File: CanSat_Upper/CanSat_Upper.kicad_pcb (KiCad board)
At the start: 2 copper layers, 50 x 50 mm, 33 parts, among them J1 SERVO1, J10 Power GND, J2 SERVO1, J3 SERVO1, J4 SERVO1, J5 SERVO1, J6 SERVO1, J7 Power 5V, J8 JST_SH_10pin, J9 JST_SH_8pin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

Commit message: LDO and gps early layout done
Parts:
- moved C6 81.3 mm to (263.8, 132.8)
- moved C5 78.2 mm to (260.8, 132.8), turned to 180 degrees
- moved C8 52.1 mm to (242.8, 91.8)
- moved C7 49.7 mm to (240.4, 107.0)
- moved C3 47.1 mm to (229.8, 121.4), turned to 180 degrees
- moved C4 43.2 mm to (226.6, 121.4)
- moved C1 42.0 mm to (220.6, 121.4), turned to 180 degrees
- moved R4 40.9 mm to (235.2, 93.4)
- moved C9 39.8 mm to (231.2, 106.0)
- moved C2 37.9 mm to (217.4, 121.4)
- moved R2 36.8 mm to (225.8, 119.0), turned to -90 degrees
- moved R3 35.4 mm to (229.8, 91.8)
- moved R1 31.5 mm to (216.6, 119.0), turned to -90 degrees
- moved U5 10.8 mm to (228.2, 119.0)
- moved U1 9.56 mm to (235.9, 100.3)
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
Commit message: general PBC layout done
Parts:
- removed C10: 100n, Capacitor_SMD:C_0603_1608Metric
- removed R2: 10k, Resistor_SMD:R_0603_1608Metric
- removed U5: LP5912_500-ma/3.3V, LDO:LP5912-LDO
- added D1: TVS, Diode_SMD:D_0402_1005Metric, F.Cu at (111.0, 100.4)
- added D2: TVS, Diode_SMD:D_0402_1005Metric, F.Cu at (112.2, 101.4)
- added D3: TVS, Diode_SMD:D_0402_1005Metric, F.Cu at (110.0, 103.6)
- added D4: TVS, Diode_SMD:D_0402_1005Metric, F.Cu at (111.0, 104.6)
- C3: value 10u -> 1u
- C4: value 10u -> 8.2p
- J10, J7: footprint Connector_Wire:SolderWirePad_1x01_SMD_4x8mm -> Connector_Wire:SolderWirePad_1x01_SMD_3x6mm
- moved C6 141.1 mm to (129.8, 88.5), turned to 180 degrees
- moved C5 135.1 mm to (133.2, 88.5), turned to 0 degrees
- moved C8 128.6 mm to (114.2, 93.6), turned to 90 degrees
- moved C7 123.5 mm to (117.8, 92.6)
- moved R4 122.7 mm to (112.5, 94.8), turned to -90 degrees
- moved C3 121.1 mm to (122.4, 65.4), turned to 90 degrees
- moved U1 119.3 mm to (116.8, 95.1), turned to 90 degrees
- moved J9 118.2 mm to (102.8, 71.4), turned to -90 degrees
- moved R3 117.5 mm to (112.5, 98.0), turned to 90 degrees
- moved C4 116.8 mm to (122.4, 68.6), turned to -90 degrees
- moved J8 116.2 mm to (103.0, 98.2), turned to -90 degrees
- moved C9 114.0 mm to (117.5, 97.6)
- moved U3 113.8 mm to (143.7, 90.5), turned to 180 degrees
- moved C1 110.2 mm to (116.4, 85.6), turned to -90 degrees
- moved U4 109.7 mm to (114.0, 87.2), turned to 90 degrees
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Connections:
- C2 pad 1: +3.3V1 -> +3.3V
- C3 pad 1: +5V -> +3.3V
- C4 pad 1: +3.3V2 -> +3.3V
- C5 pad 1: +3.3V1 -> +3.3V
- C6 pad 1: +3.3V1 -> +3.3V
- C8 pad 1: +3.3V2 -> +3.3V
- C9 pad 1: +3.3V2 -> +3.3V
- J8 pad 8: /GPS_TX -> /GPS_RX
- J8 pad 9: /GPS_RX -> /GPS_TX
- R1 pad 2: +3.3V1 -> +3.3V
- R3 pad 1: +3.3V2 -> +3.3V
- R4 pad 1: +3.3V2 -> +3.3V
- U1 pad 13: +3.3V2 -> +3.3V
- U1 pad 2: +3.3V2 -> +3.3V
- U2 pad 1: +3.3V2 -> +3.3V
- U3 pad 52: +3.3V1 -> +3.3V
- U3 pad 53: +3.3V1 -> +3.3V
- U4 pad 1: +3.3V1 -> +3.3V
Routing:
- net +3.3V: track 0.00 -> 91.3 mm
- net /XBEE_TX: track 0.00 -> 49.4 mm
- net /XBEE_RX: track 0.00 -> 49.3 mm
- net /GPS_TX: track 0.00 -> 23.6 mm
- net /GPS_RX: track 0.00 -> 23.3 mm
- net /S4: track 0.00 -> 12.2 mm
- net /S3: track 0.00 -> 12.2 mm
- net /SCL: track 0.00 -> 12.1 mm
- net /SDA: track 0.00 -> 11.4 mm
- net /S2: track 0.00 -> 8.63 mm
- net /S5: track 0.00 -> 8.52 mm
- net /S1: track 0.00 -> 3.87 mm
- net /S6: track 0.00 -> 3.81 mm
- net Net-(U4-PG): track 0.00 -> 1.50 mm
- net Net-(U1-C1): track 0.00 -> 1.31 mm
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- added copper zone on F.Cu, net +5V
- added copper zone on B.Cu, net GND
- added copper zone on F.Cu, net GND

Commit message: v0.1 finished
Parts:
- R3, R4: value 4.7k -> 10k
- moved D2 8.61 mm to (107.8, 94.0), turned to -90 degrees
- moved D1 5.28 mm to (107.8, 96.2)
- moved J9 0.48 mm to (103.3, 71.4)
- moved J8 0.30 mm to (103.3, 98.2)
- moved C7 0.24 mm to (117.8, 92.4)
- moved 3 0.20 mm to (112.4, 68.5)
- moved 4 0.20 mm to (112.4, 74.4)
- moved 5 0.20 mm to (116.2, 68.5)
- moved 6 0.20 mm to (116.2, 74.4)
- moved C8 0.20 mm to (114.0, 93.6)
- moved 1 0.20 mm to (108.6, 68.5)
- moved 2 0.20 mm to (108.6, 74.4)
- moved C9 0.16 mm to (117.5, 97.8)
- renumbered J1 to 1, J6 to 2, J2 to 3, J5 to 4, J3 to 5, J4 to 6
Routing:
- net /S1: track 3.87 -> 2.96 mm
- net GND: vias 120 -> 238
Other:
- board text added: "+5V"
- board text added: "-1 -2 -GND -3 -4 -GND -5 -6"
- board text added: "-SDA -GND -SCL -GND -XBEE_TX -XBEE_RX -GND -GPS_RX -GPS_TX -GND"
- board text added: "GND"
- board text added: "GND +5V PWM"
- board text added: "KRAKAN UPPER_BOARD v0.1 FLIP MAJEWSKI majewski0filip@gmail.com"
- board text added: "PWM +5V GND"
- board text added: "S"

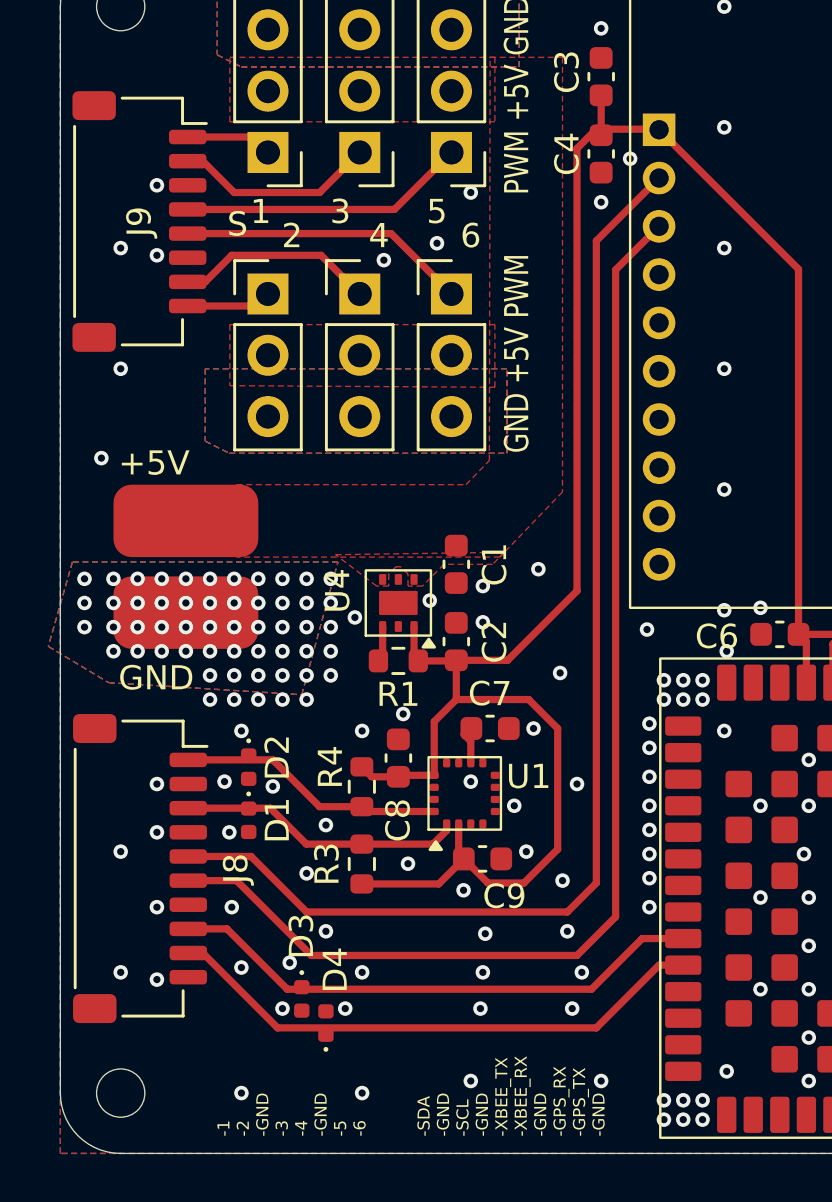
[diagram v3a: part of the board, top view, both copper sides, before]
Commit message: Added variations of the magnetometers power supply
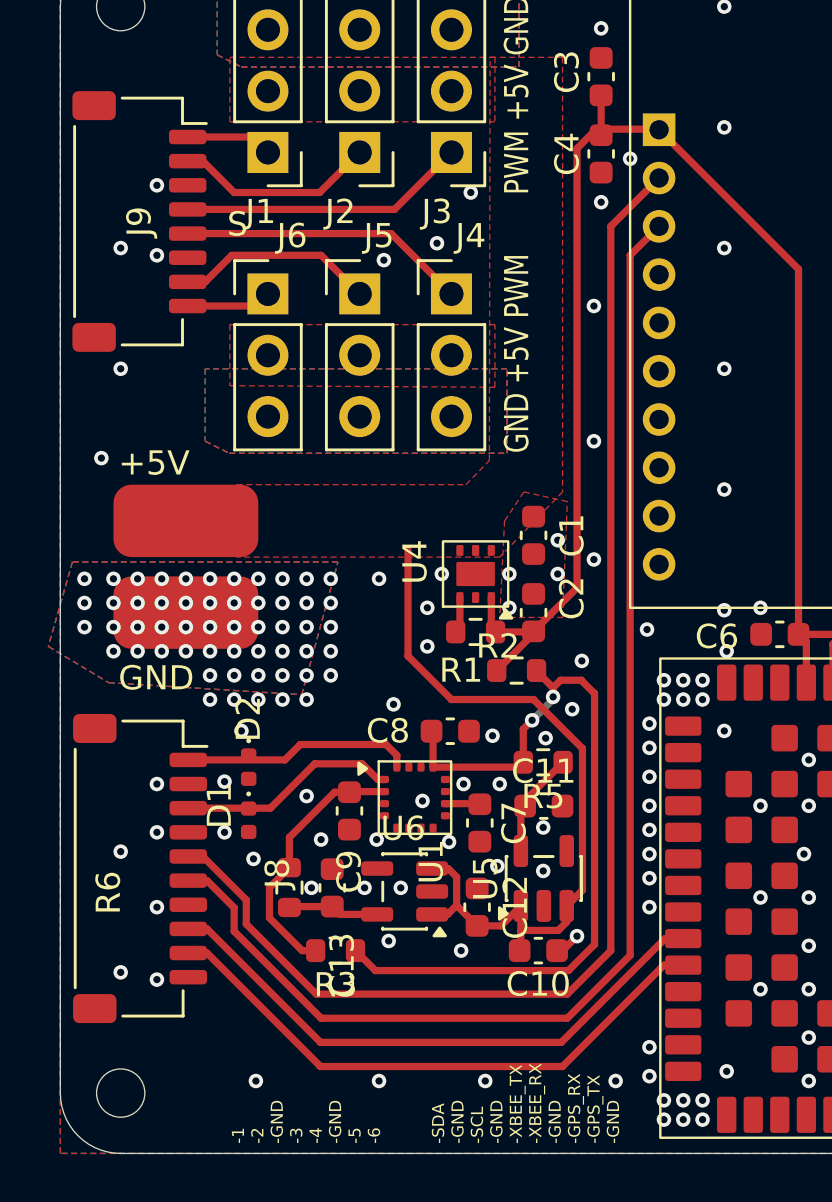
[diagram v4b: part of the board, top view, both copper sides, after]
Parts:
- removed D3, D4: TVS, Diode_SMD:D_0402_1005Metric
- removed R4: 10k, Resistor_SMD:R_0603_1608Metric
- added C10: 1u, Capacitor_SMD:C_0603_1608Metric, F.Cu at (119.8, 101.6)
- added C11: 1u, Capacitor_SMD:C_0603_1608Metric, F.Cu at (120.0, 95.6)
- added C12: 1u, Capacitor_SMD:C_0603_1608Metric, F.Cu at (117.3, 99.8)
- added C13: 1u, Capacitor_SMD:C_0603_1608Metric, F.Cu at (111.3, 99.0)
- added R2: 0, Resistor_SMD:R_0603_1608Metric, F.Cu at (118.9, 90.0)
- added R5: 0, Resistor_SMD:R_0603_1608Metric, F.Cu at (120.0, 93.8)
- added R6: 0, Resistor_SMD:R_0603_1608Metric, F.Cu at (109.5, 99.0)
- added U5: TPS77033PDBV, Package_TO_SOT_SMD:SOT-23-5, F.Cu at (120.0, 98.6)
- added U6: TPS77033PDBV, Package_TO_SOT_SMD:SOT-23-5, F.Cu at (114.3, 99.2)
- R3: value 10k -> 0
- moved C9 5.86 mm to (112.0, 95.8), turned to -90 degrees
- moved C7 3.94 mm to (117.4, 96.3), turned to -90 degrees
- moved R3 3.75 mm to (111.4, 101.6), turned to 180 degrees
- moved U4 3.42 mm to (117.2, 86.0)
- moved R1 3.42 mm to (117.2, 88.4)
- moved C2 3.42 mm to (119.6, 87.6)
- moved C1 3.42 mm to (119.6, 84.4)
- moved C8 2.42 mm to (116.2, 92.5), turned to 0 degrees
- moved U1 2.07 mm to (114.7, 95.3), turned to 0 degrees
- renumbered 1 to J1, 3 to J2, 5 to J3, 6 to J4, 4 to J5, 2 to J6
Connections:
- C8 pad 1: +3.3V -> Net-(U1-DVDD)
- C9 pad 1: +3.3V -> Net-(U1-AVDD)
- R3 pad 1: +3.3V -> Net-(U1-DVDD)
- R3 pad 2: /SCL -> Net-(U1-AVDD)
- U1 pad 13: +3.3V -> Net-(U1-DVDD)
- U1 pad 2: +3.3V -> Net-(U1-AVDD)
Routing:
- net Net-(U1-DVDD): track 0.00 -> 33.3 mm, vias 0 -> 2
- net +5V: track 0.00 -> 31.5 mm
- net +3.3V: track 91.2 -> 61.1 mm
- net Net-(U1-AVDD): track 0.00 -> 10.8 mm
- net /XBEE_TX: track 49.4 -> 54.5 mm
- net +3.3V2: track 0.00 -> 4.40 mm
- net +3.3V3: track 0.00 -> 3.73 mm
- net /XBEE_RX: track 49.3 -> 53.0 mm
- net /SCL: track 12.1 -> 9.46 mm
- net /GPS_TX: track 23.6 -> 25.5 mm
- net /SDA: track 11.4 -> 9.58 mm
- net /GPS_RX: track 23.3 -> 24.9 mm
- net GND: track 0.00 -> 1.07 mm, vias 238 -> 241
